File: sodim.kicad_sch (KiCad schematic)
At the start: 6 parts

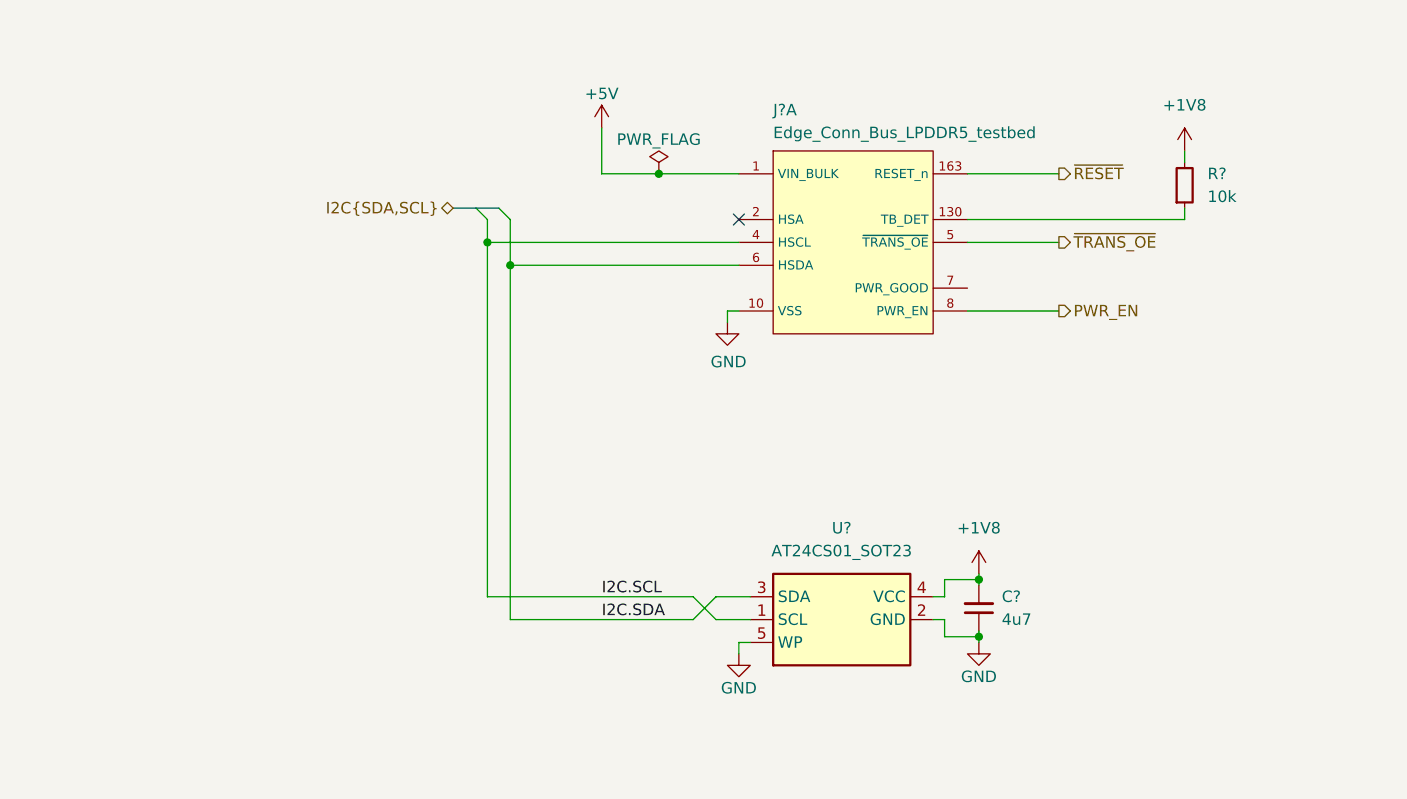
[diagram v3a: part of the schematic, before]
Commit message: [#52536] schematics: update I2C connection
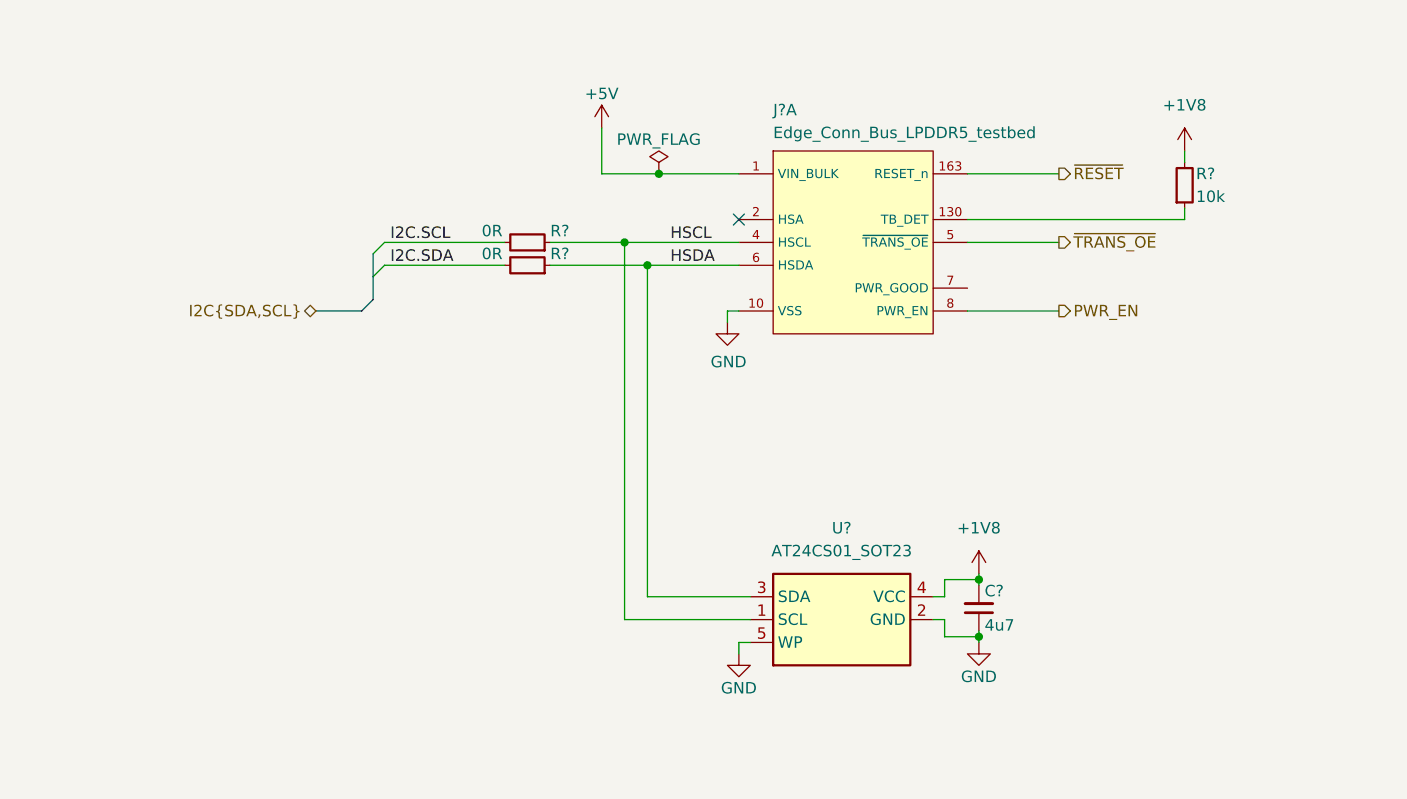
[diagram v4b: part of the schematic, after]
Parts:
- removed J?: Edge_Conn_Bus_LPDDR5_testbed, antmicro-footprints:Edge_Conn_Bus_DDR5_SODIMM, symbol antmicroMemoryConnectorsPCCardSockets:Edge_Conn_Bus_LPDDR5_testbed
- added J?: Edge_Conn_Bus_LPDDR5_testbed, antmicro-footprints:Edge_Conn_Bus_DDR5_SODIMM, symbol antmicroMemoryConnectorsPCCardSockets:Edge_Conn_Bus_LPDDR5_testbed
- added R? (x2): R_0R_0402, antmicro-footprints:R_0402_1005Metric, symbol antmicroResistors0402:R_0R_0402
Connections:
- net DMI0_DIR_A: now also J?.120 (DMI0_DIR_A)
- net DMI1_DIR_A: now also J?.121 (DMI1_DIR_A)
- net DQH_DIR_A: now also J?.54 (DQH_DIR_A)
- net DQL_DIR_A: now also J?.53 (DQL_DIR_A)
- net I2C.SCL: now also R?.2; no longer J?.4 (HSCL), U?.1 (SCL)
- net I2C.SDA: now also R?.2; no longer J?.6 (HSDA), U?.3 (SDA)
- net LPDDR5_HV_A.CA0: now also J?.107 (CA0_A)
- net LPDDR5_HV_A.CA1: now also J?.109 (CA1_A)
- net LPDDR5_HV_A.CA2: now also J?.113 (CA2_A)
- net LPDDR5_HV_A.CA3: now also J?.114 (CA3_A)
- net LPDDR5_HV_A.CA4: now also J?.115 (CA4_A)
- net LPDDR5_HV_A.CA5: now also J?.116 (CA5_A)
- net LPDDR5_HV_A.CA6: now also J?.119 (CA6_A)
- net LPDDR5_HV_A.CK_N: now also J?.133 (CK_C_A)
- net LPDDR5_HV_A.CK_P: now also J?.131 (CK_T_A)
- net LPDDR5_HV_A.CS0: now also J?.106 (CS0_A)
- net LPDDR5_HV_A.CS1: now also J?.110 (CS1_A)
- net LPDDR5_HV_A.DMI0: now also J?.19 (DMI0_A)
- net LPDDR5_HV_A.DMI1: now also J?.42 (DMI1_A)
- net LPDDR5_HV_A.DQ0: now also J?.11 (DQ0_A)
- net LPDDR5_HV_A.DQ1: now also J?.12 (DQ1_A)
- net LPDDR5_HV_A.DQ10: now also J?.35 (DQ10_A)
- net LPDDR5_HV_A.DQ11: now also J?.38 (DQ11_A)
- net LPDDR5_HV_A.DQ12: now also J?.45 (DQ12_A)
- net LPDDR5_HV_A.DQ13: now also J?.46 (DQ13_A)
- net LPDDR5_HV_A.DQ14: now also J?.49 (DQ14_A)
- net LPDDR5_HV_A.DQ15: now also J?.50 (DQ15_A)
- net LPDDR5_HV_A.DQ2: now also J?.15 (DQ2_A)
- net LPDDR5_HV_A.DQ3: now also J?.16 (DQ3_A)
- net LPDDR5_HV_A.DQ4: now also J?.23 (DQ4_A)
- net LPDDR5_HV_A.DQ5: now also J?.26 (DQ5_A)
- net LPDDR5_HV_A.DQ6: now also J?.27 (DQ6_A)
- net LPDDR5_HV_A.DQ7: now also J?.30 (DQ7_A)
- net LPDDR5_HV_A.DQ8: now also J?.31 (DQ8_A)
- net LPDDR5_HV_A.DQ9: now also J?.34 (DQ9_A)
- net LPDDR5_HV_A.RDQS0_N: now also J?.20 (RDQS0_C_A)
- net LPDDR5_HV_A.RDQS0_P: now also J?.22 (RDQS0_T_A)
- net LPDDR5_HV_A.RDQS1_N: now also J?.39 (RDQS1_C_A)
- net LPDDR5_HV_A.RDQS1_P: now also J?.41 (RDQS1_T_A)
- net LPDDR5_HV_A.WCK0_N: now also J?.62 (WCK0_C_A)
- net LPDDR5_HV_A.WCK0_P: now also J?.64 (WCK0_T_A)
- net LPDDR5_HV_A.WCK1_N: now also J?.81 (WCK1_C_A)
- net LPDDR5_HV_A.WCK1_P: now also J?.83 (WCK1_T_A)
- new net HSCL: J?.4 (HSCL), R?.1, U?.1 (SCL)
- new net HSDA: J?.6 (HSDA), R?.1, U?.3 (SDA)

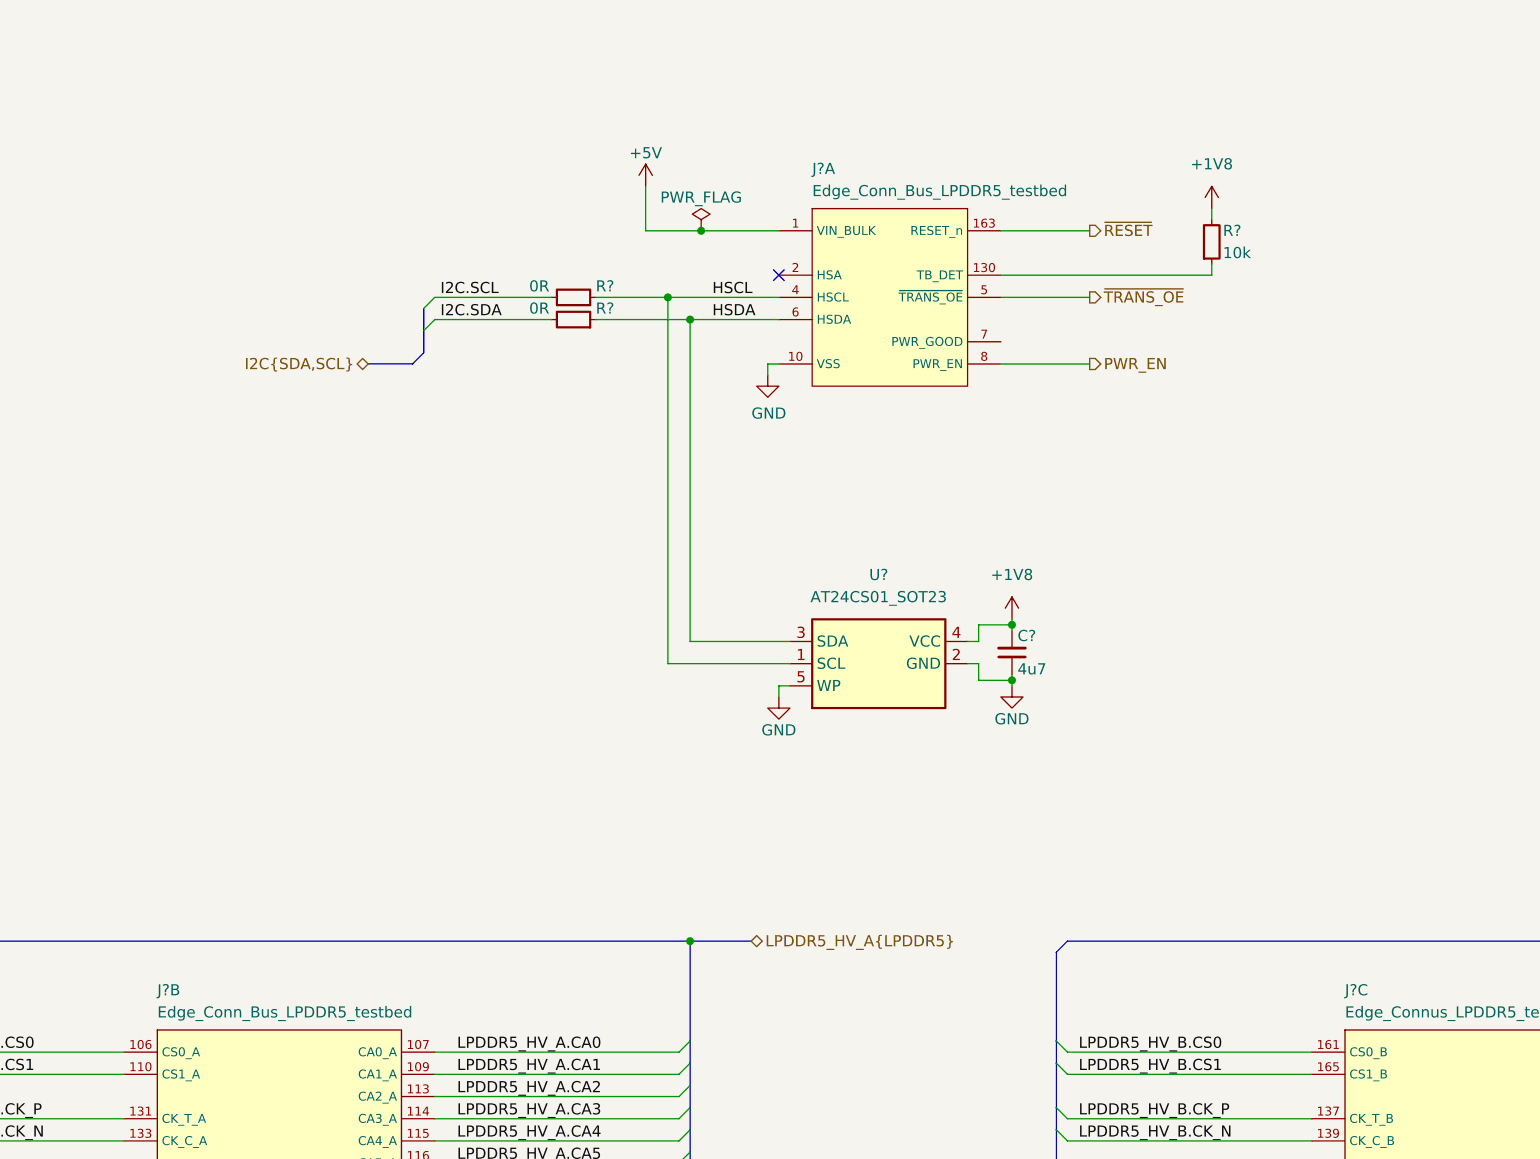
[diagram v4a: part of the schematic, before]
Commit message: [#52835] schematics: update components after standardization
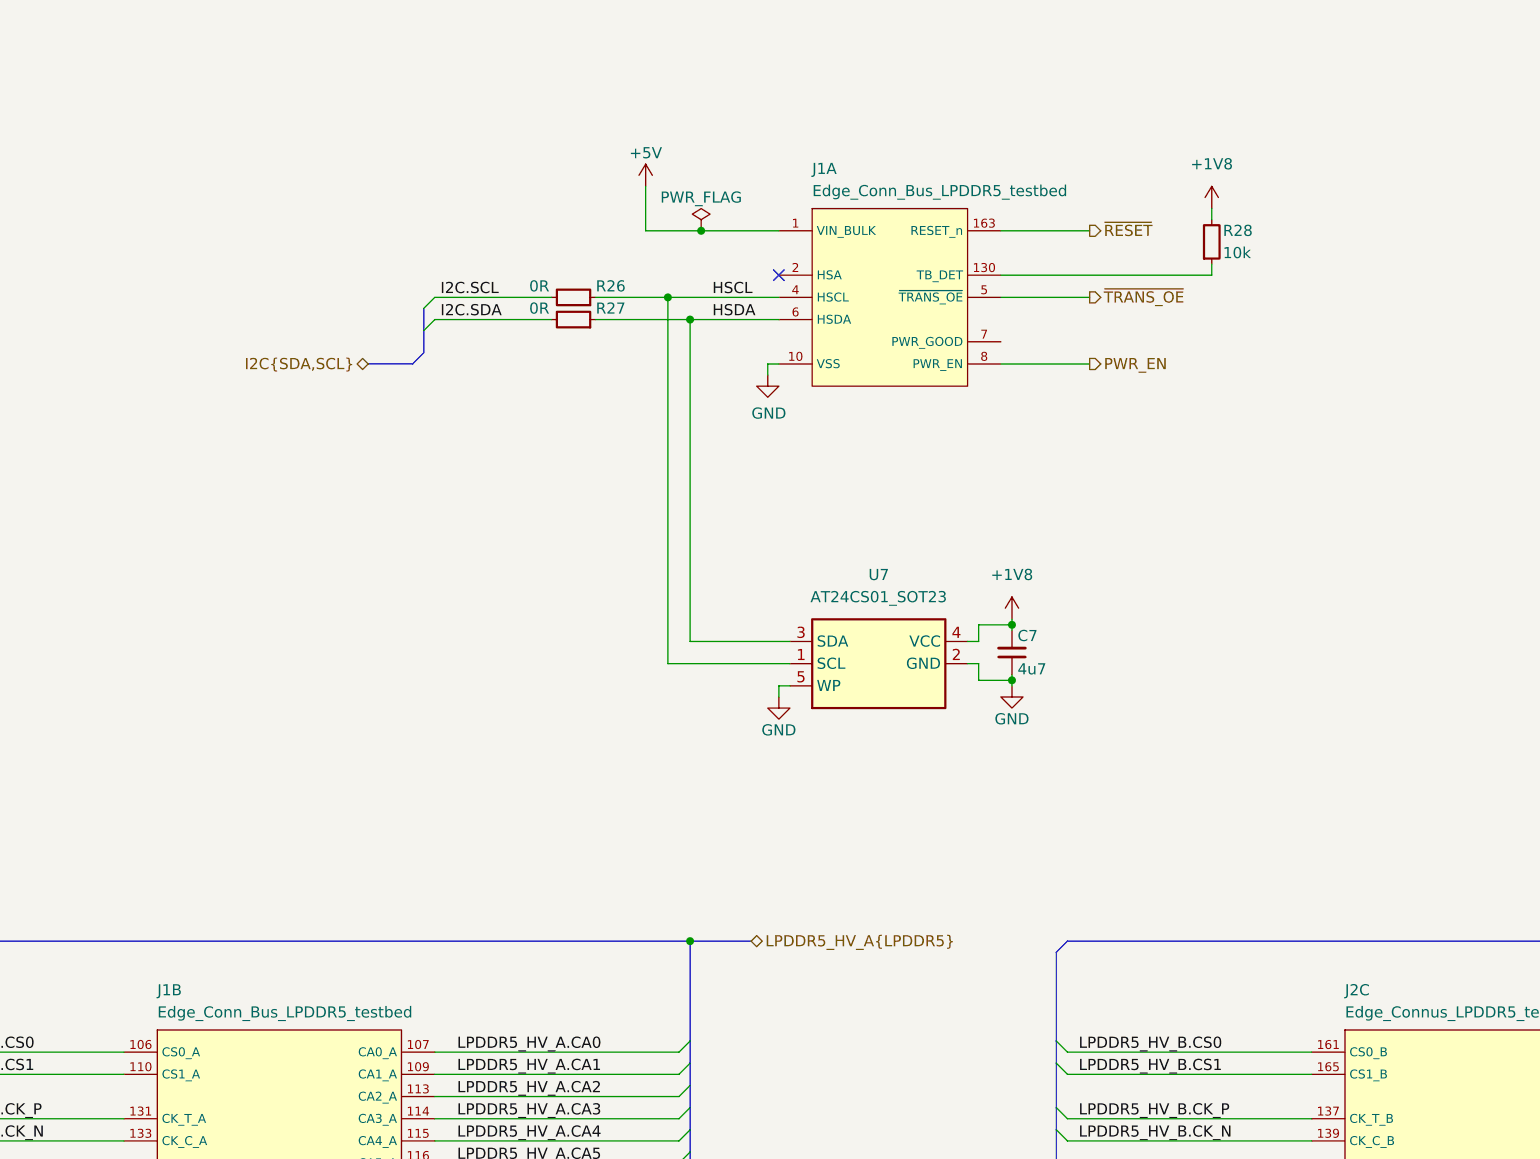
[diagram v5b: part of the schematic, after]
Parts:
- gave numbers to parts that had none: 7
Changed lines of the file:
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@@
   (symbol (lib_id "antmicropower:+1V8") (at 242.57 46.99 0) (unit 1)
     (in_bom yes) (on_board yes) (fields_autoplaced)
-    (property "Reference" "#PWR?" (id 0) (at 257.81 49.53 0)
+    (property "Reference" "#PWR0143" (id 0) (at 257.81 49.53 0)
       (effects (font (size 1.27 1.27) (thickness 0.15)) (justify left bottom) hide)
     )
@@
   (symbol (lib_id "antmicroMemoryConnectorsPCCardSockets:Edge_Conn_Bus_LPDDR5_testbed") (at 118.11 143.51 0) (unit 2)
     (in_bom yes) (on_board yes)
-    (property "Reference" "J?" (id 0) (at 121.92 137.16 0)
+    (property "Reference" "J1" (id 0) (at 121.92 137.16 0)
       (effects (font (size 1.27 1.27)) (justify left bottom))
     )
@@
   (symbol (lib_id "antmicroMemoryConnectorsPCCardSockets:Edge_Conn_Bus_LPDDR5_testbed") (at 254 143.51 0) (unit 3)
     (in_bom yes) (on_board yes)
-    (property "Reference" "J?" (id 0) (at 257.81 137.16 0)
+    (property "Reference" "J2" (id 0) (at 257.81 137.16 0)
       (effects (font (size 1.27 1.27)) (justify left bottom))
     )
@@
   (symbol (lib_id "antmicroResistors0402:R_0R_0402") (at 172.085 59.69 180) (unit 1)
     (in_bom yes) (on_board yes)
-    (property "Reference" "R?" (id 0) (at 172.085 58.42 0)
+    (property "Reference" "R27" (id 0) (at 172.085 58.42 0)
       (effects (font (size 1.27 1.27) (thickness 0.15)) (justify right))
     )
@@
   (symbol (lib_id "antmicroResistors0402:R_0R_0402") (at 172.085 57.15 180) (unit 1)
     (in_bom yes) (on_board yes)
-    (property "Reference" "R?" (id 0) (at 172.085 55.88 0)
+    (property "Reference" "R26" (id 0) (at 172.085 55.88 0)
       (effects (font (size 1.27 1.27) (thickness 0.15)) (justify right))
     )
@@
   (symbol (lib_id "antmicropower:+5V") (at 177.8 44.45 0) (unit 1)
     (in_bom yes) (on_board yes)
-    (property "Reference" "#PWR?" (id 0) (at 193.04 46.99 0)
+    (property "Reference" "#PWR0142" (id 0) (at 193.04 46.99 0)
       (effects (font (size 1.27 1.27) (thickness 0.15)) (justify left bottom) hide)
     )
@@
   (symbol (lib_id "antmicropower:+1V8") (at 219.71 93.98 0) (unit 1)
     (in_bom yes) (on_board yes) (fields_autoplaced)
-    (property "Reference" "#PWR?" (id 0) (at 234.95 96.52 0)
+    (property "Reference" "#PWR0140" (id 0) (at 234.95 96.52 0)
       (effects (font (size 1.27 1.27) (thickness 0.15)) (justify left bottom) hide)
     )
@@
   (symbol (lib_id "antmicroCapacitors0402:C_4u7_0402") (at 219.71 100.33 90) (unit 1)
     (in_bom yes) (on_board yes)
-    (property "Reference" "C?" (id 0) (at 220.345 95.885 90)
+    (property "Reference" "C7" (id 0) (at 220.345 95.885 90)
       (effects (font (size 1.27 1.27) (thickness 0.15)) (justify right))
     )
@@
   (symbol (lib_id "lpddr5-sodimm:GND") (at 193.04 102.87 0) (unit 1)
     (in_bom yes) (on_board yes)
-    (property "Reference" "#PWR?" (id 0) (at 193.04 109.22 0)
+    (property "Reference" "#PWR0141" (id 0) (at 193.04 109.22 0)
       (effects (font (size 1.27 1.27)) hide)
     )
@@
   (symbol (lib_id "antmicroResistors0402:R_10k_0402") (at 242.57 53.34 90) (unit 1)
     (in_bom yes) (on_board yes)
-    (property "Reference" "R?" (id 0) (at 243.84 49.53 90)
+    (property "Reference" "R28" (id 0) (at 243.84 49.53 90)
       (effects (font (size 1.27 1.27) (thickness 0.15)) (justify right))
     )
@@
   (symbol (lib_id "lpddr5-sodimm:GND") (at 219.71 101.6 0) (mirror y) (unit 1)
     (in_bom yes) (on_board yes)
-    (property "Reference" "#PWR?" (id 0) (at 219.71 107.95 0)
+    (property "Reference" "#PWR0139" (id 0) (at 219.71 107.95 0)
       (effects (font (size 1.27 1.27)) hide)
     )
@@
   (symbol (lib_id "antmicroMemoryConnectorsPCCardSockets:Edge_Conn_Bus_LPDDR5_testbed") (at 193.04 49.53 0) (unit 1)
     (in_bom yes) (on_board yes)
-    (property "Reference" "J?" (id 0) (at 196.85 43.18 0)
+    (property "Reference" "J1" (id 0) (at 196.85 43.18 0)
       (effects (font (size 1.27 1.27)) (justify left bottom))
     )
@@
   (symbol (lib_id "antmicroMemory:AT24CS01_SOT23") (at 194.31 96.52 0) (unit 1)
     (in_bom yes) (on_board yes) (fields_autoplaced)
-    (property "Reference" "U?" (id 0) (at 204.47 88.9 0)
+    (property "Reference" "U7" (id 0) (at 204.47 88.9 0)
       (effects (font (size 1.27 1.27) (thickness 0.15)))
     )
